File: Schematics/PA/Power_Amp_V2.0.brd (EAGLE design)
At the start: 50.5 x 78.1 mm, 109 parts, among them J1 4_PIN_AMPCONN, J10 OSTVN03A150, J11 OSTVN03A150, J12 OSTVN03A150, J13 OSTVN03A150, J14 OSTVN03A150, J2 1984633, J3 2TERMINAL_SPEAKER, J4 2TERMINAL_SPEAKER, J5 2TERMINAL_SPEAKER, J6 OSTVN03A150, J7 OSTVN03A150, J8 OSTVN03A150, J9 OSTVN03A150, U1 LME49830, U2 LME49830, U3 LME49830

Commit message: small changes to logo
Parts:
- moved U$48 0.66 mm to (35.6, 74.2)
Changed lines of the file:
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@@
 <grid distance="0.003125" unitdist="mic" unit="inch" style="lines" multiple="1" display="yes" altdistance="0.025" altunitdist="inch" altunit="inch"/>
 <layers>
-<layer number="1" name="Top" color="4" fill="1" visible="no" active="yes"/>
-<layer number="16" name="Bottom" color="1" fill="1" visible="no" active="yes"/>
+<layer number="1" name="Top" color="4" fill="1" visible="yes" active="yes"/>
+<layer number="16" name="Bottom" color="1" fill="1" visible="yes" active="yes"/>
 <layer number="17" name="Pads" color="2" fill="1" visible="yes" active="yes"/>
 <layer number="18" name="Vias" color="2" fill="1" visible="yes" active="yes"/>
@@
 <wire x1="50.47" y1="78.105" x2="1.27" y2="78.105" width="0" layer="20"/>
 <wire x1="0" y1="76.5175" x2="0" y2="0" width="0" layer="20"/>
-<text x="30.043725" y="75.73103125" size="0.889" layer="21" font="vector" ratio="15">Power Amplifier</text>
+<text x="30.112565625" y="76.62565625" size="0.889" layer="21" font="vector" ratio="15">Power Amplifier</text>
 <text x="31.913615625" y="73.064490625" size="0.889" layer="21" font="vector" ratio="15">CT
 CM</text>
@@
 <wire x1="42.874946875" y1="52.071228125" x2="42.874946875" y2="61.11535625" width="2.159" layer="30"/>
 <wire x1="42.874946875" y1="61.11535625" x2="42.997178125" y2="61.20335625" width="2.032" layer="30"/>
-<text x="42.618134375" y="71.365584375" size="1.524" layer="21" rot="R90">GM-+</text>
+<text x="42.618134375" y="71.365584375" size="1.27" layer="21" rot="R90">GM-+</text>
 <text x="42.734415625" y="4.807346875" size="1.778" layer="21" rot="R90">L</text>
 <text x="39.945378125" y="26.134459375" size="1.778" layer="21" rot="R90">B</text>
@@
 </element>
 <element name="U$17" library="PersonalLogos" package="MUSHROOM" value="" x="11.737865625" y="76.558996875" rot="R180"/>
-<element name="U$48" library="PersonalLogos" package="SPEAKER" value="" x="35.271303125" y="73.650784375"/>
+<element name="U$48" library="PersonalLogos" package="SPEAKER" value="" x="35.581084375" y="74.23573125"/>
 <element name="J6" library="Amplifier_Parts" package="OSTVN03A150" value="OSTVN03A150" x="37.753165625" y="50.79018125" rot="R90"/>
 <element name="J7" library="Amplifier_Parts" package="OSTVN03A150" value="OSTVN03A150" x="37.7327625" y="59.07185625" rot="R90"/>

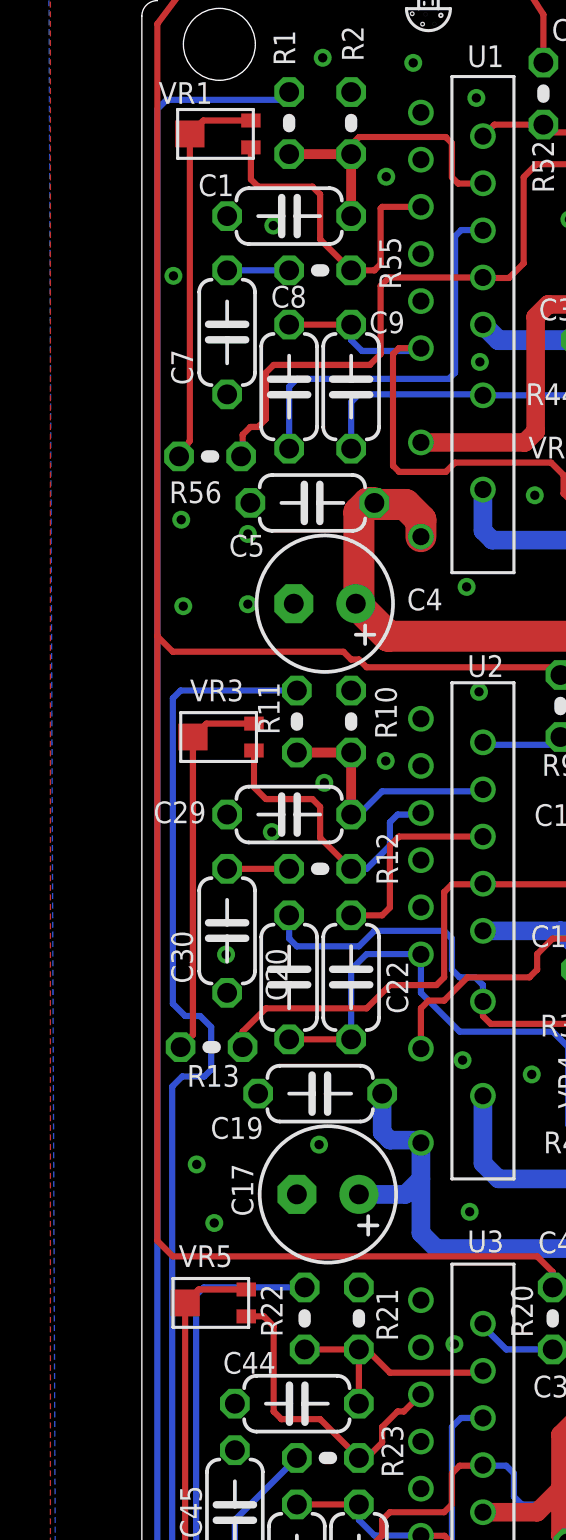
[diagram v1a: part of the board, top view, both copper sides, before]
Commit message: small changes to silk screen
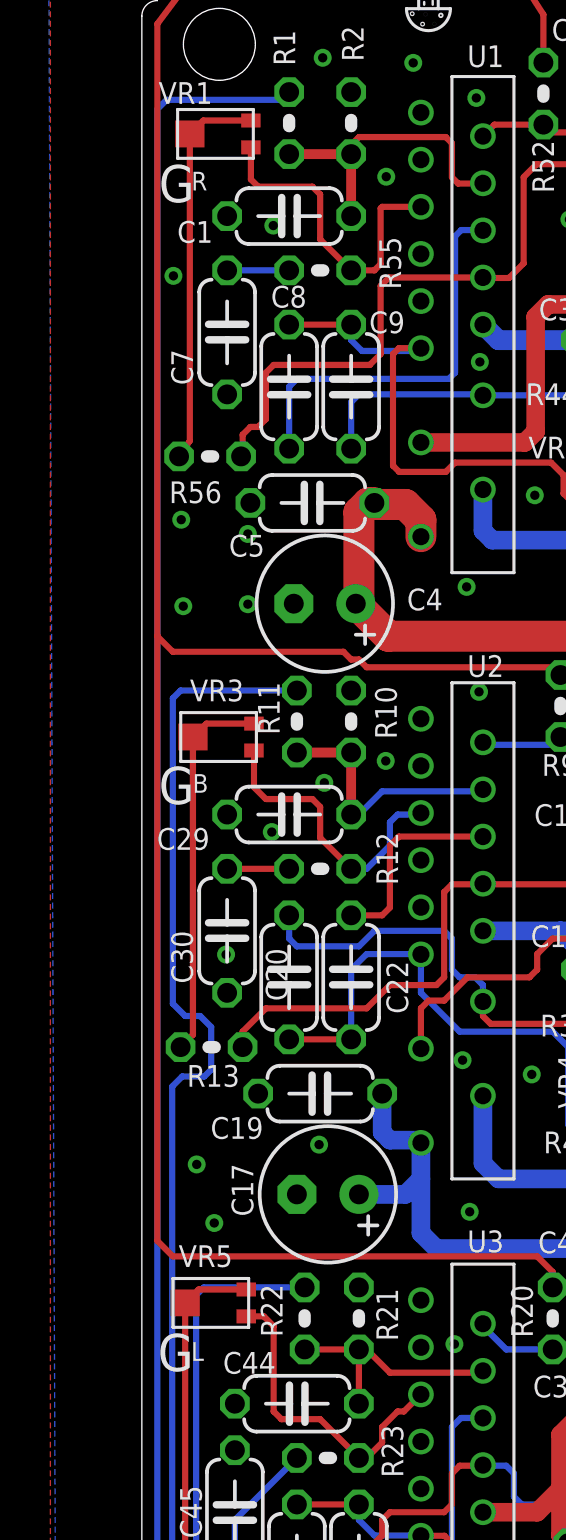
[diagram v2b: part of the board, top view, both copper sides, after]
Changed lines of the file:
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@@
 <wire x1="43.156515625" y1="38.11846875" x2="43.156515625" y2="28.969115625" width="2.032" layer="30"/>
 <wire x1="43.156515625" y1="28.969115625" x2="44.055784375" y2="28.069846875" width="2.032" layer="30"/>
+<text x="0.6966625" y="68.89460625" size="1.524" layer="21">G</text>
+<text x="0.69286875" y="44.244184375" size="1.524" layer="21">G</text>
+<text x="0.6555625" y="21.02028125" size="1.524" layer="21">G</text>
+<text x="2.078409375" y="44.707784375" size="0.762" layer="21">B</text>
+<text x="2.0277" y="69.377984375" size="0.762" layer="21">R</text>
+<text x="2.018378125" y="21.4403375" size="0.762" layer="21">L</text>
 </plain>
 <attributes>
@@
 <elements>
 <element name="C1" library="rcl" package="C050-024X044" value="0.1uF" x="6.0325" y="68.326" smashed="yes">
-<attribute name="NAME" x="2.3103125" y="69.144253125" size="0.889" layer="25" font="vector" ratio="15"/>
+<attribute name="NAME" x="1.446625" y="67.23285625" size="0.889" layer="25" font="vector" ratio="15"/>
 <attribute name="VALUE" x="3.8735" y="65.659" size="1.27" layer="27" ratio="10"/>
 </element>
@@
 </element>
 <element name="C29" library="rcl" package="C050-024X044" value="22pF" x="6.0325" y="43.815" smashed="yes">
-<attribute name="NAME" x="0.4726125" y="43.46060625" size="0.889" layer="25" font="vector" ratio="15"/>
+<attribute name="NAME" x="0.615975" y="42.37134375" size="0.889" layer="25" font="vector" ratio="15"/>
 <attribute name="VALUE" x="3.8735" y="41.148" size="1.27" layer="27" ratio="10"/>
 </element>

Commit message: Final PA update before PCB order
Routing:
- net V-: track 195.2 -> 193.4 mm
- net L_VBE_E: track 48.9 -> 48.3 mm
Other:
- board text added: "Bias"
- board text added: "Gain"
